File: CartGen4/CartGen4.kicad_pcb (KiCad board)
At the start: 4 copper layers, 52.8 x 60.9 mm, 77 parts, among them J1 MEM2080-00-128-00-A, SW1 SW_Push, U1 TPS65266-1RHBR, U10 IS25WP080D-JNLE, U11 DS1391U-33+, U2 SN74LV1T34DCKR, U3 SIT8008BI-73-33E-33.333333G, U4 NXS0108BQX, U5 AS1C8M16PL-70BIN, U6 NXS0108BQX, U7 NXS0108BQX, U8 NXS0104BQX, U9 LFXP2-8E-5MN132C, Y1 FC-135R 32.7680KA-E5

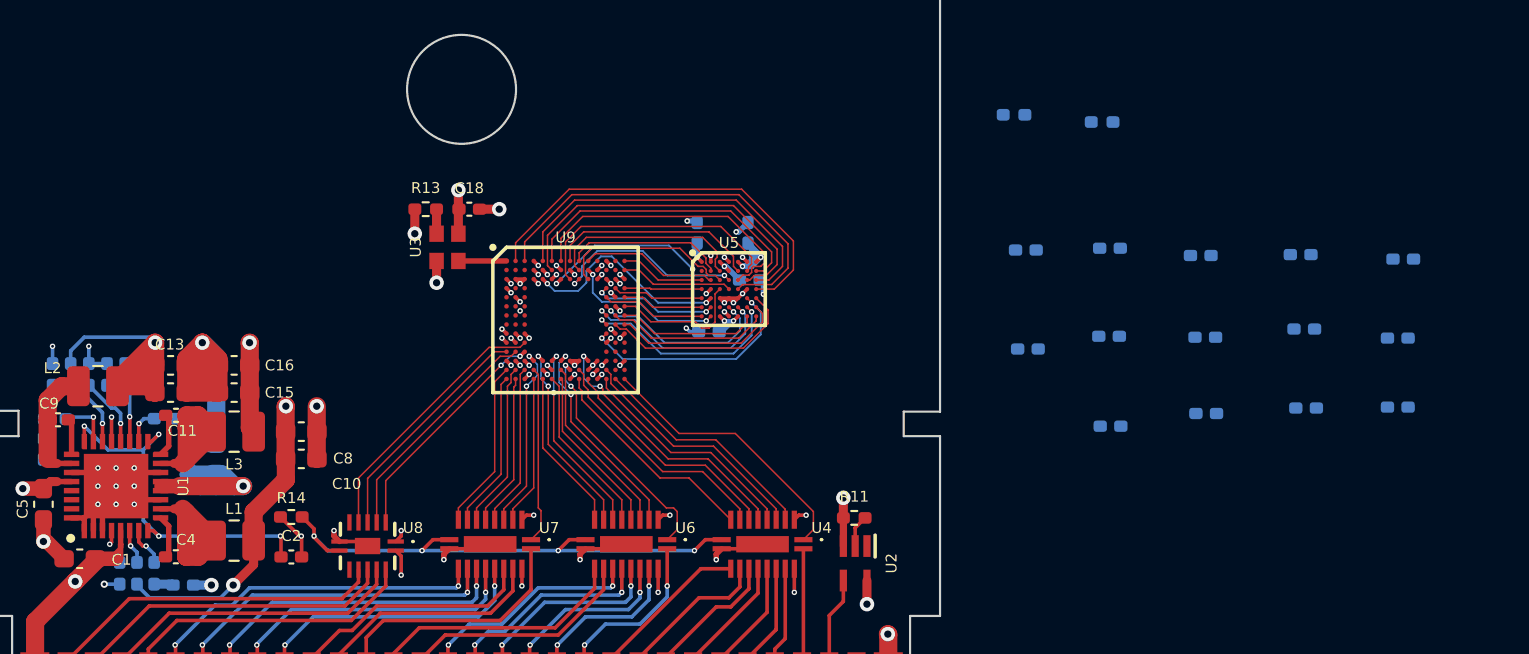
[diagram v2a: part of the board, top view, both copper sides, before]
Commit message: Wired FPGA decoupling caps
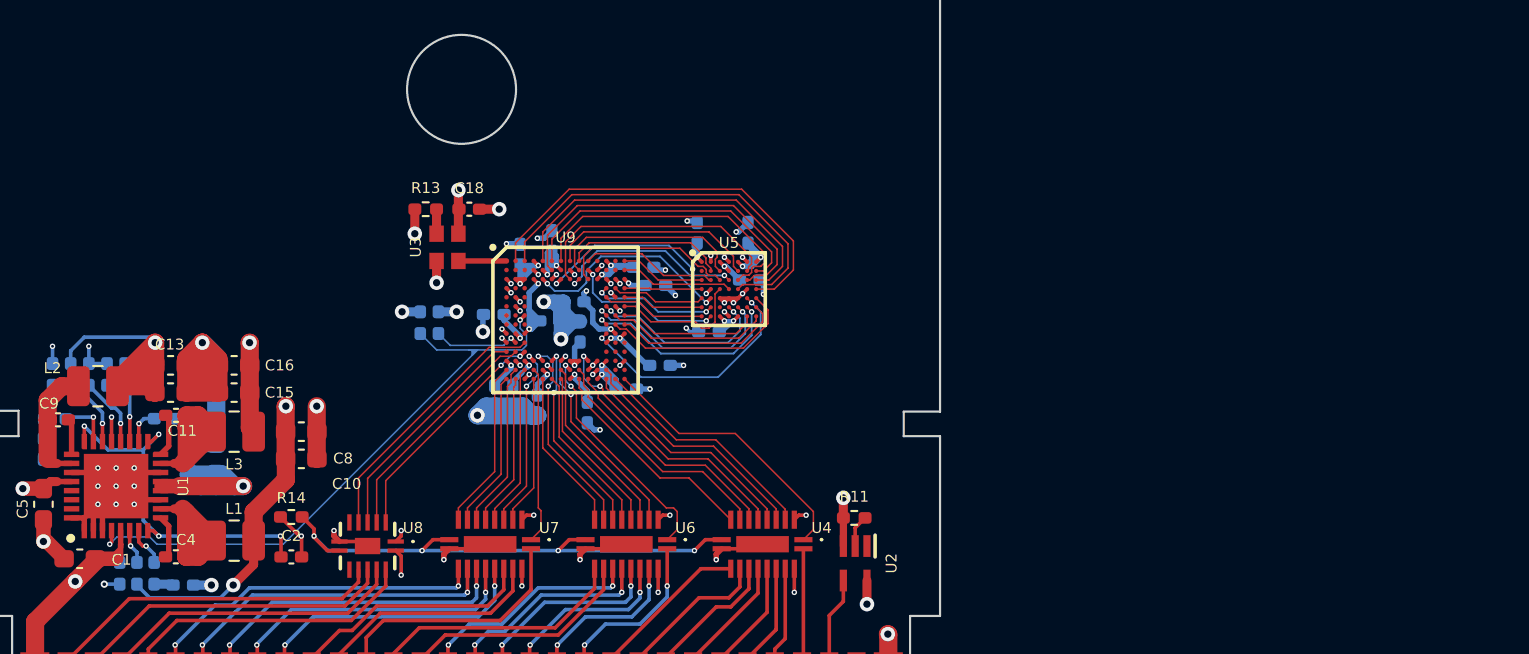
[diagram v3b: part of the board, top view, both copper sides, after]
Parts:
- moved C19 50.0 mm to (67.8, 73.3)
- moved C30 46.9 mm to (71.0, 69.3), turned to 90 degrees
- moved C22 41.5 mm to (70.9, 73.7), turned to 0 degrees
- moved C32 41.2 mm to (76.7, 71.8), turned to 0 degrees
- moved C20 40.8 mm to (72.2, 72.7)
- moved C24 40.2 mm to (73.0, 78.8), turned to -90 degrees
- moved C21 38.8 mm to (69.2, 70.0), turned to 90 degrees
- moved R15 38.2 mm to (64.8, 73.8), turned to -90 degrees
- moved C25 37.5 mm to (70.2, 78.3), turned to -90 degrees
- moved C31 34.8 mm to (67.8, 77.8), turned to -90 degrees
- moved R12 34.6 mm to (63.8, 73.8), turned to -90 degrees
- moved C36 33.0 mm to (68.8, 77.8), turned to -90 degrees
- moved C23 31.2 mm to (76.0, 70.8), turned to 0 degrees
- moved C37 29.7 mm to (72.5, 74.3), turned to 90 degrees
- moved C38 23.3 mm to (75.1, 77.5), turned to 0 degrees
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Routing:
- net PS_PGOOD: track 0.79 -> 34.4 mm, vias 1 -> 2
- net +3V3: track 14.4 -> 36.8 mm, vias 19 -> 20
- net GND: track 86.7 -> 108.2 mm, vias 54 -> 65
- net +1V2: track 20.5 -> 30.9 mm, vias 7 -> 9
- net Net-(R15-Pad2): track 0.35 -> 4.79 mm
- net +1V8: track 33.1 -> 37.2 mm
- net RAM_UB#: track 12.4 -> 13.3 mm

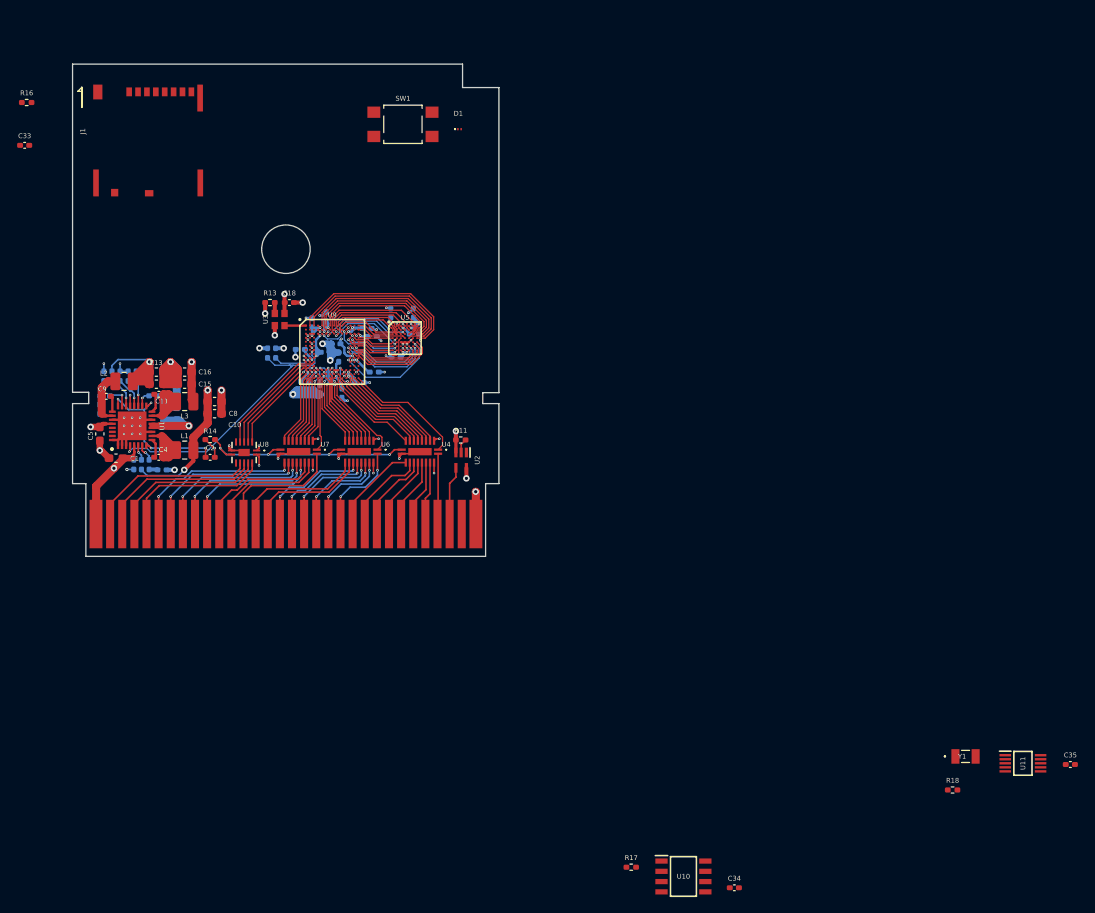
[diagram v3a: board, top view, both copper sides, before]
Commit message: Planned rough location of SPI peripherals
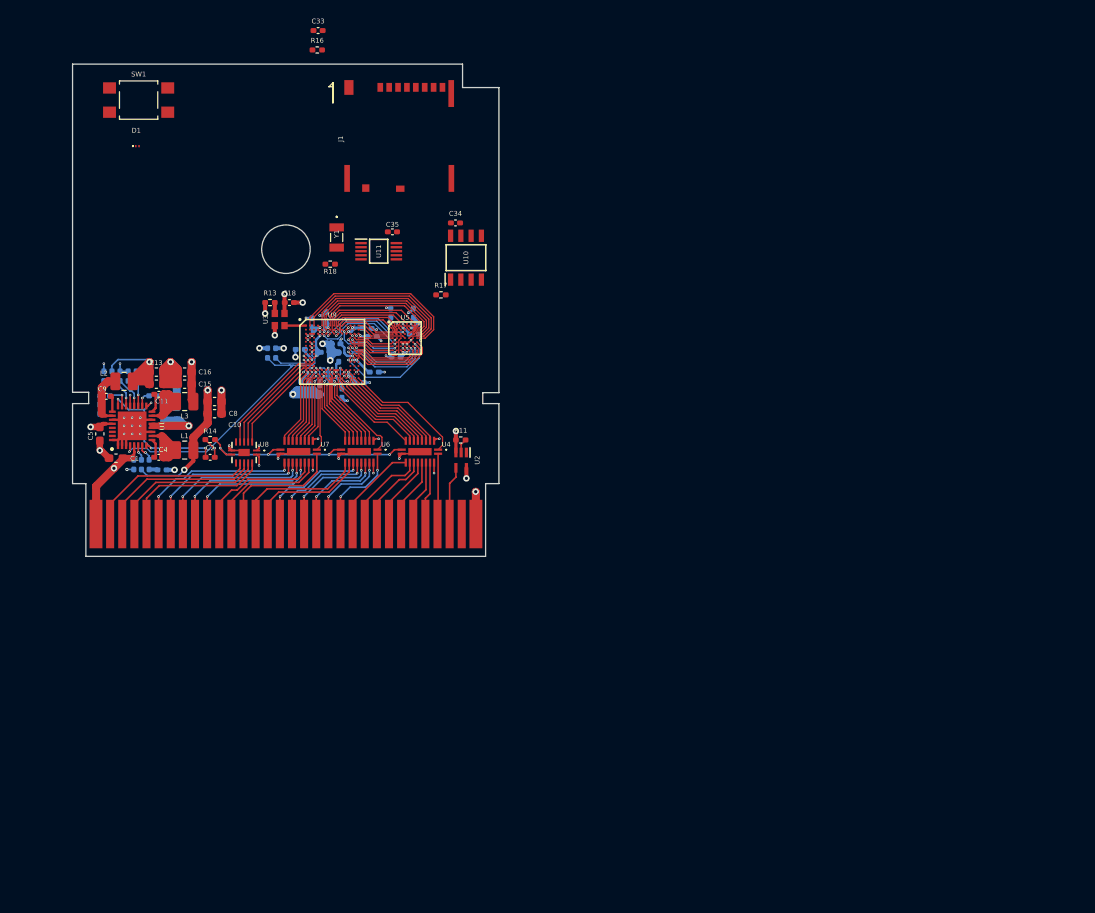
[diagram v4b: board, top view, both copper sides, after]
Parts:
- moved C35 106.7 mm to (79.2, 58.8), turned to 180 degrees
- moved U11 101.8 mm to (77.5, 61.2)
- moved Y1 100.9 mm to (72.3, 59.5), turned to -90 degrees
- moved R18 100.8 mm to (71.5, 62.8)
- moved C34 89.2 mm to (87.0, 57.7)
- moved U10 81.1 mm to (88.3, 62.0), turned to 90 degrees
- moved R17 74.6 mm to (85.2, 66.6)
- moved D1 39.9 mm to (47.5, 48.2)
- moved C33 39.0 mm to (70.0, 33.9)
- moved R16 36.5 mm to (69.9, 36.3)
- moved SW1 32.8 mm to (47.8, 42.5)
- moved J1 25.7 mm to (77.3, 40.4)
- moved BT1 3.61 mm to (62.4, 46.8)
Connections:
- Y1 pad 1: (no net) -> Net-(U11-Pad1)

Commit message: Reviewed cartridge edge clearances
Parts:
- moved BT1 4.20 mm to (62.4, 51.0)
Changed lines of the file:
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@@
       (effects (font (size 1 1) (thickness 0.15)))
     )
-    (fp_line (start 24.35 19.1) (end 26.35 19.1) (layer "Edge.Cuts") (width 0.12))
-    (fp_line (start -24.4 17.7) (end -24.4 19.1) (layer "Edge.Cuts") (width 0.12))
+    (fp_line (start -24.6 -17.1) (end -24.6 -21.1) (layer "Dwgs.User") (width 0.12))
+    (fp_line (start -24.6 -21.1) (end 20.05 -21.1) (layer "Dwgs.User") (width 0.12))
+    (fp_line (start 20.05 -18.2) (end 24.55 -18.2) (layer "Dwgs.User") (width 0.12))
+    (fp_line (start 20.05 -21.1) (end 20.05 -18.2) (layer "Dwgs.User") (width 0.12))
+    (fp_line (start 24.55 -18.2) (end 24.55 -14.2) (layer "Dwgs.User") (width 0.12))
+    (fp_poly (pts
+        (xy 20.05 -14.2)
+        (xy 24.55 -14.2)
+        (xy 24.55 15.95)
+        (xy 24.55 17.75)
+        (xy 24.55 19.1)
+        (xy 24.55 20.9)
+        (xy 24.55 28)
+        (xy -24.6 28)
+        (xy -24.6 20.45)
+        (xy -24.6 19.1)
+        (xy -24.6 17.7)
+        (xy -24.6 15.95)
+        (xy -24.6 -17.1)
+        (xy 20.05 -17.1)
+      ) (layer "Dwgs.User") (width 0.12) (fill none))
+    (fp_line (start -26.4 19.1) (end -24.4 19.1) (layer "Edge.Cuts") (width 0.12))
+    (fp_line (start 24.35 17.75) (end 24.35 19.1) (layer "Edge.Cuts") (width 0.12))
+    (fp_line (start -24.75 29) (end -24.75 38) (layer "Edge.Cuts") (width 0.12))
+    (fp_line (start -26.4 -22.9) (end 21.85 -22.9) (layer "Edge.Cuts") (width 0.12))
+    (fp_line (start 26.35 19.1) (end 26.35 29) (layer "Edge.Cuts") (width 0.12))
+    (fp_line (start -26.4 17.7) (end -26.4 -22.9) (layer "Edge.Cuts") (width 0.12))
+    (fp_line (start 24.7 29) (end 24.7 38) (layer "Edge.Cuts") (width 0.12))
+    (fp_line (start -26.4 19.1) (end -26.4 29) (layer "Edge.Cuts") (width 0.12))
+    (fp_line (start 24.35 17.75) (end 26.35 17.75) (layer "Edge.Cuts") (width 0.12))
     (fp_line (start -26.4 29) (end -24.75 29) (layer "Edge.Cuts") (width 0.12))
-    (fp_line (start 26.35 19.1) (end 26.35 29) (layer "Edge.Cuts") (width 0.12))
-    (fp_line (start 24.35 17.75) (end 26.35 17.75) (layer "Edge.Cuts") (width 0.12))
-    (fp_line (start -24.75 29) (end -24.75 38) (layer "Edge.Cuts") (width 0.12))
-    (fp_line (start 24.7 29) (end 24.7 38) (layer "Edge.Cuts") (width 0.12))
-    (fp_line (start 24.35 17.75) (end 24.35 19.1) (layer "Edge.Cuts") (width 0.12))
+    (fp_line (start 21.85 -20) (end 26.35 -20) (layer "Edge.Cuts") (width 0.12))
     (fp_line (start 21.85 -22.9) (end 21.85 -20) (layer "Edge.Cuts") (width 0.12))
     (fp_line (start 26.35 29) (end 24.7 29) (layer "Edge.Cuts") (width 0.12))
-    (fp_line (start 21.85 -20) (end 26.35 -20) (layer "Edge.Cuts") (width 0.12))
-    (fp_line (start -26.4 17.7) (end -26.4 -22.9) (layer "Edge.Cuts") (width 0.12))
+    (fp_line (start -24.4 17.7) (end -24.4 19.1) (layer "Edge.Cuts") (width 0.12))
+    (fp_line (start -24.4 17.7) (end -26.4 17.7) (layer "Edge.Cuts") (width 0.12))
+    (fp_line (start 24.35 19.1) (end 26.35 19.1) (layer "Edge.Cuts") (width 0.12))
+    (fp_line (start 26.35 -20) (end 26.35 17.75) (layer "Edge.Cuts") (width 0.12))
     (fp_line (start 24.7 38) (end -24.75 38) (layer "Edge.Cuts") (width 0.12))
-    (fp_line (start -26.4 19.1) (end -26.4 29) (layer "Edge.Cuts") (width 0.12))
-    (fp_line (start -26.4 19.1) (end -24.4 19.1) (layer "Edge.Cuts") (width 0.12))
-    (fp_line (start -24.4 17.7) (end -26.4 17.7) (layer "Edge.Cuts") (width 0.12))
-    (fp_line (start -26.4 -22.9) (end 21.85 -22.9) (layer "Edge.Cuts") (width 0.12))
-    (fp_line (start 26.35 -20) (end 26.35 17.75) (layer "Edge.Cuts") (width 0.12))
     (fp_circle (center 0 0) (end 3 0) (layer "Edge.Cuts") (width 0.12) (fill none))
     (pad "1" smd rect (at -23.5 34) (size 1.6 6) (layers "F.Cu" "F.Paste" "F.Mask")
@@
   )
   (footprint "Battery:Battery_CR1225" (layer "F.Cu")
-    (at 62.4 46.8)
+    (at 62.4 51)
     (descr "CR1225 battery")
     (tags "battery CR1225 coin cell")
